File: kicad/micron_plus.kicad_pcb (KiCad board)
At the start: 2 copper layers, 163.8 x 123.2 mm, 91 parts, among them J1 Conn_02x17_Odd_Even, J2 Cliff DC10A, Q1 2N2905A, Q2 2N2905A, Q3 2N3904, Q4 2N3904, U1 MC68A21, U10 74LS00, U11 7406, U12 HM6264LP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

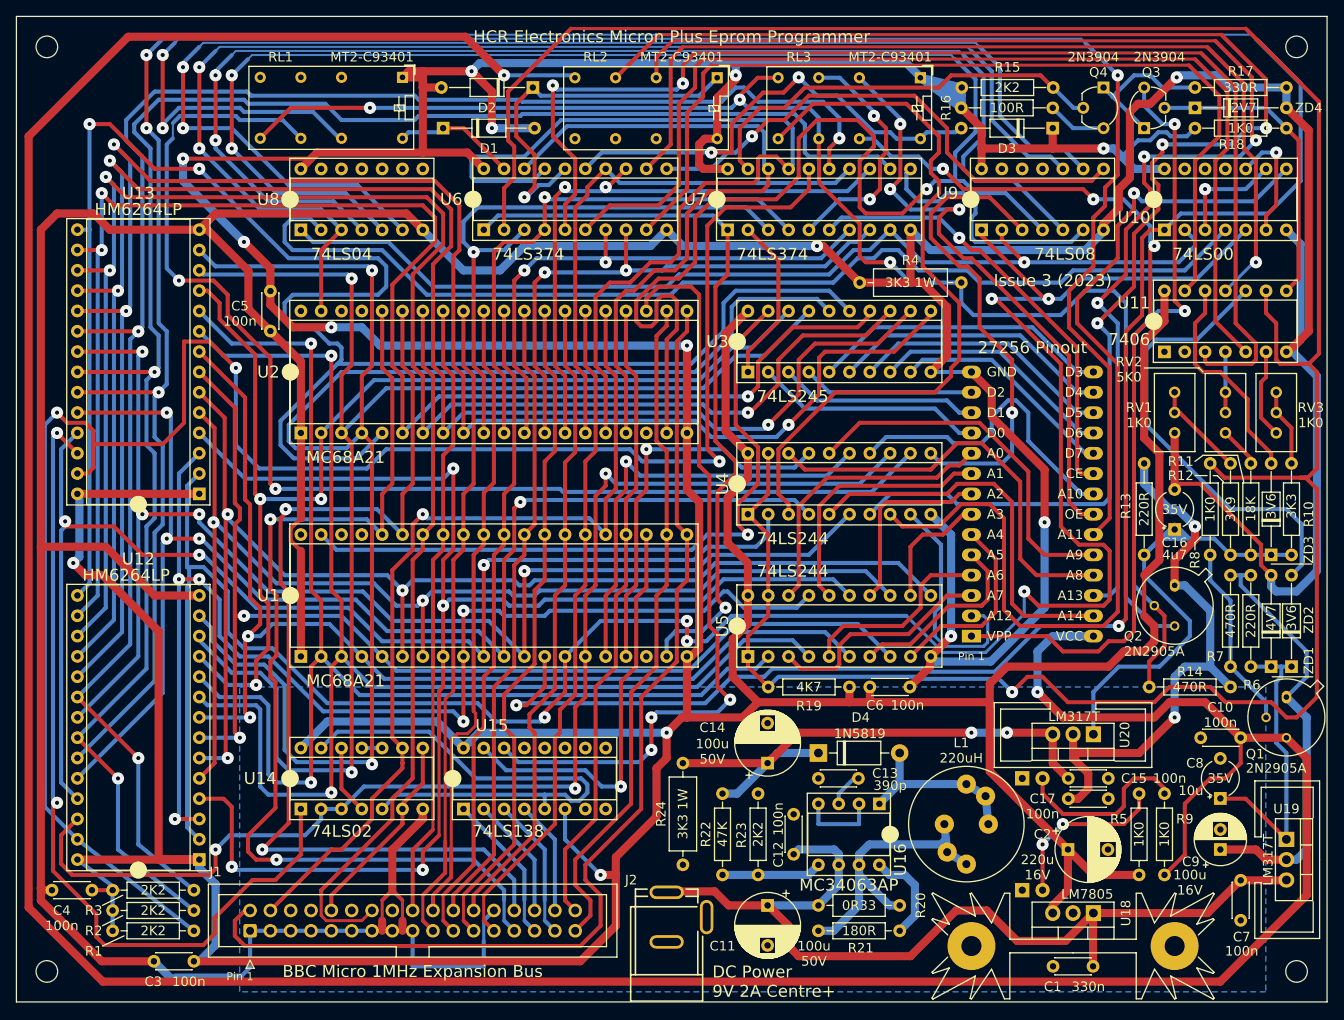
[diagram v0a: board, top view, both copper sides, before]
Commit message: KiCAD: Improve ground routing
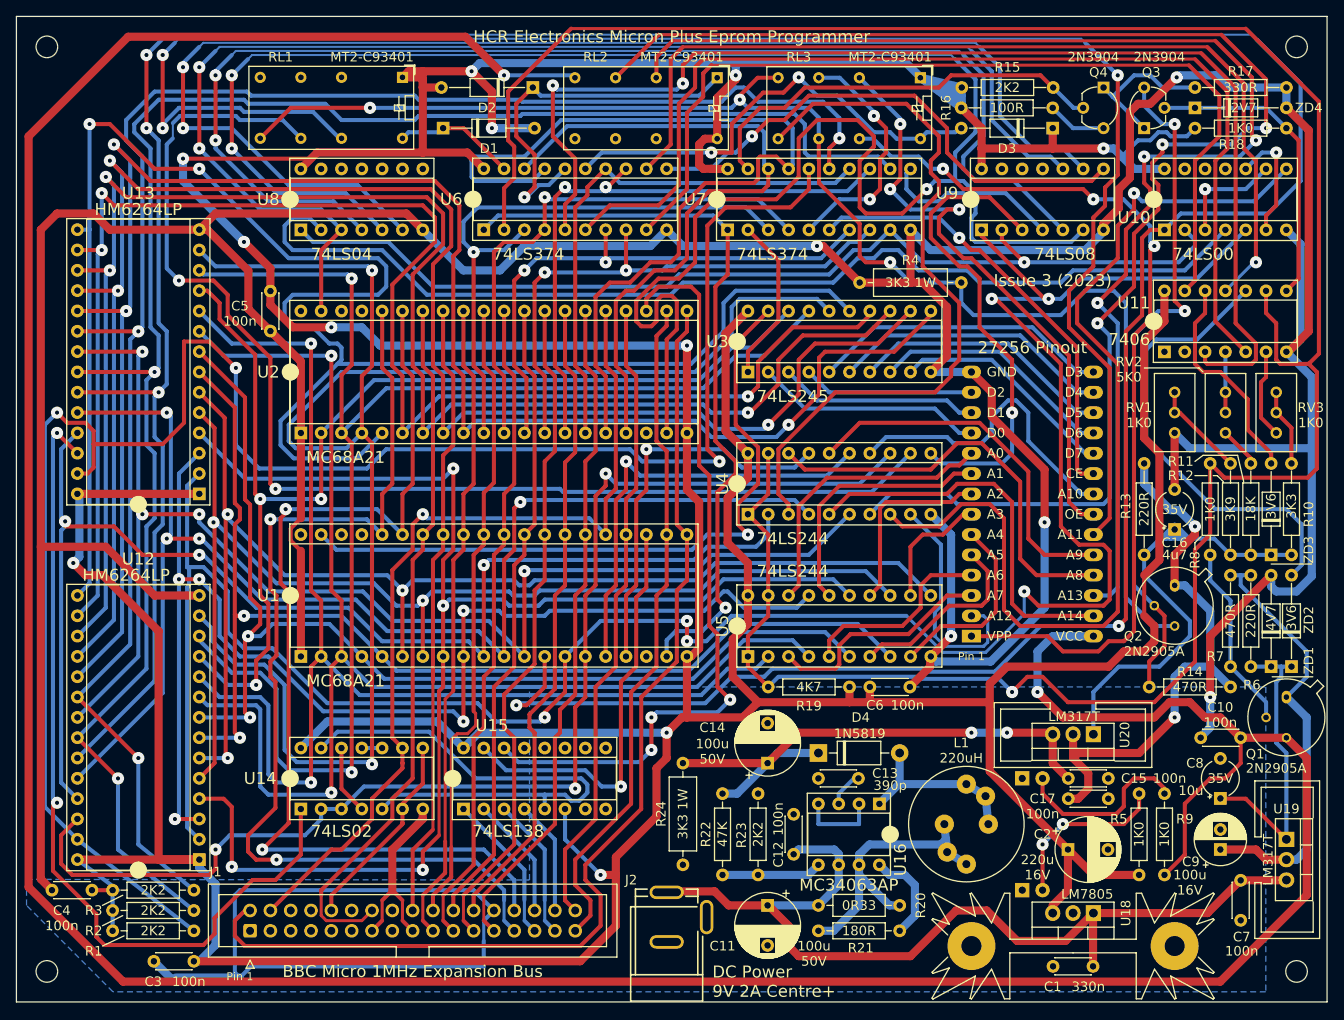
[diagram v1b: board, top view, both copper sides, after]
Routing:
- net GND: track 676.4 -> 716.3 mm, vias 4 -> 5
- net /Control Latches/nVCCEnable: track 338.8 -> 319.1 mm
- net /Main Logic and Eprom Socket/EpromVCC: track 430.5 -> 429.0 mm
- net Net-(U11-Pad10): track 56.3 -> 57.5 mm

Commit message: KiCAD: Holes now M3, inset 4.25mm X and 3.7mm Y
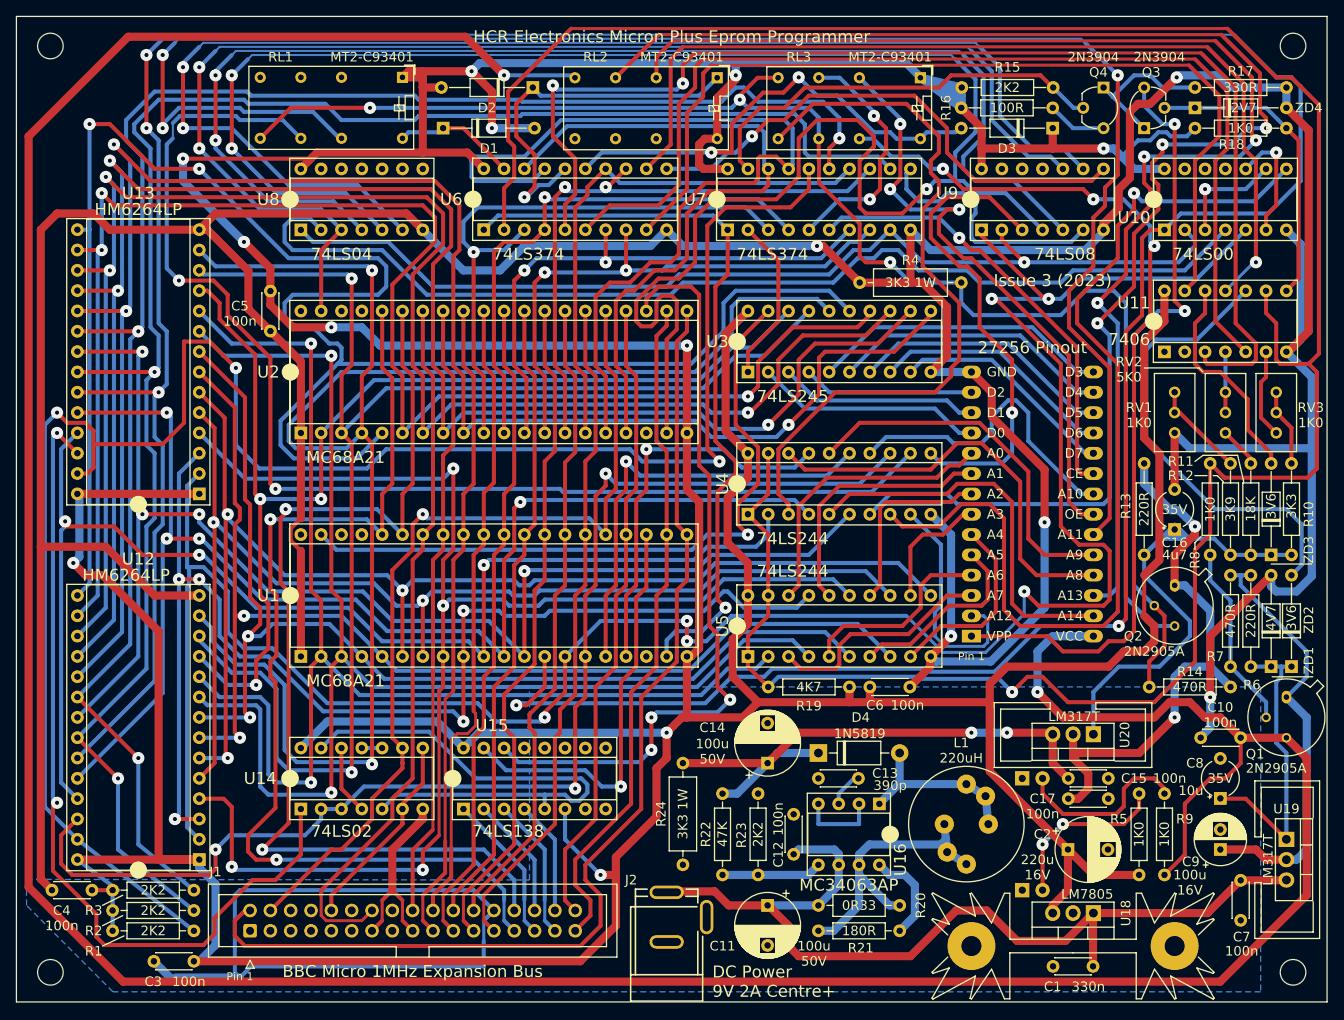
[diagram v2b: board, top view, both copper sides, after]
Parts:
- H1, H2, H3, H4: footprint MountingHole:MountingHole_2.7mm_M2.5 -> MountingHole:MountingHole_3.2mm_M3
- moved H3 0.45 mm to (44.9, 141.1)
- moved H4 0.45 mm to (200.2, 141.1)
- moved H1 0.45 mm to (44.9, 25.3)
- moved H2 0.45 mm to (200.2, 25.3)

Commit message: KiCAD: Add JLCJLCJLCJLC
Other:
- board text added: "JLCJLCJLCJLC"
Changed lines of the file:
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@@
     (effects (font (size 1.5 1.5) (thickness 0.2)) (justify mirror))
+  )
+  (gr_text "JLCJLCJLCJLC" (at 167.64 64.135) (layer "B.SilkS")
+    (effects (font (size 1.2 1.2) (thickness 0.15)) (justify mirror))
   )
   (gr_text "2732\n27513" (at 90.805 66.04) (layer "B.SilkS")

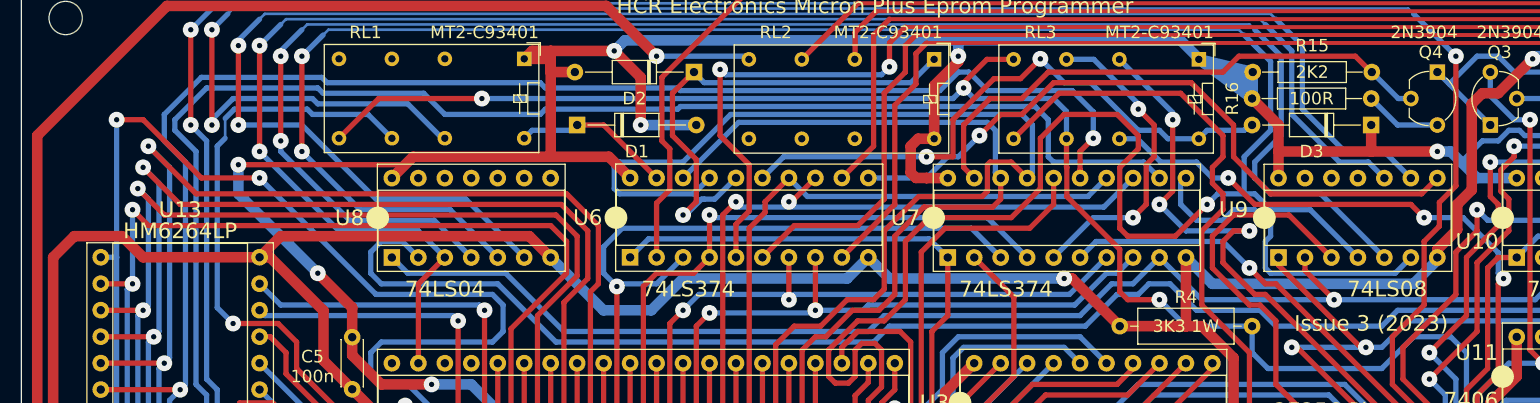
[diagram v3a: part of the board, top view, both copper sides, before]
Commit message: KiCAD: Add (c) Hoglet
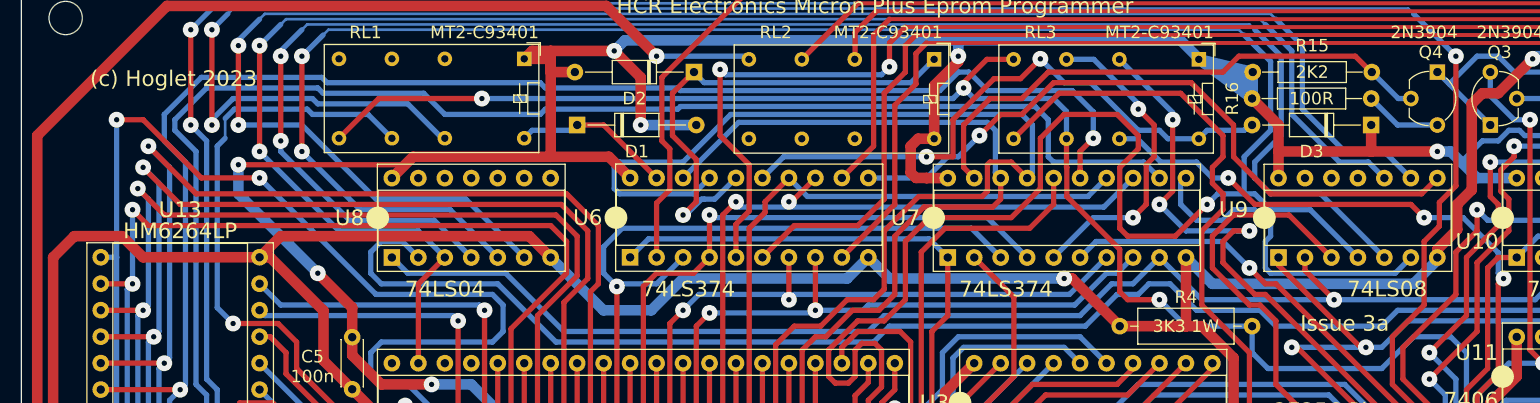
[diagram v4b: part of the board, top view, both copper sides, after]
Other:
- board text added: "(c) Hoglet 2023"
- board text added: "Issue 3a"
- board text removed: "Issue 3 (2023)"
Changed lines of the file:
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@@
     (effects (font (size 1.5 1.5) (thickness 0.2)) (justify left mirror))
   )
-  (gr_text "Issue 3 (2023)" (at 169.545 54.61) (layer "B.SilkS")
+  (gr_text "Issue 3a" (at 167.64 54.61) (layer "B.SilkS")
     (effects (font (size 1.5 1.5) (thickness 0.2)) (justify mirror))
   )
@@
     (effects (font (size 1.5 1.5) (thickness 0.2)) (justify mirror))
   )
-  (gr_text "Issue 3 (2023)" (at 170.18 54.61) (layer "F.SilkS")
+  (gr_text "(c) Hoglet 2023" (at 55.245 31.115) (layer "B.SilkS")
+    (effects (font (size 1.5 1.5) (thickness 0.2)) (justify mirror))
+  )
+  (gr_text "Issue 3a" (at 167.64 54.61) (layer "F.SilkS")
     (effects (font (size 1.5 1.5) (thickness 0.2)))
   )
@@
     (effects (font (size 1.2 1.2) (thickness 0.15)))
   )
+  (gr_text "(c) Hoglet 2023" (at 55.245 31.115) (layer "F.SilkS")
+    (effects (font (size 1.5 1.5) (thickness 0.2)))
+  )
   (gr_text "A7" (at 161.925 93.98) (layer "F.SilkS")

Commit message: KiCAD: Setup Solder Mask Clearance for JLC
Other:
- rule pad_to_mask_clearance: 0 -> 0.05
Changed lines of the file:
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@@
       (dielectric_constraints no)
     )
-    (pad_to_mask_clearance 0)
+    (pad_to_mask_clearance 0.05)
+    (solder_mask_min_width 0.1)
     (grid_origin 40.64 144.78)
     (pcbplotparams
